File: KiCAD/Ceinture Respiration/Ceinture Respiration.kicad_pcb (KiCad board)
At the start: 2 copper layers, 124 x 55 mm, 37 parts, among them J1 DIN-8, J2 DIN-8, J3 Conn_01x04, J4 MEM2061-01-188-00-A_REVA, J5 Conn_01x02, J7 Conn_01x10_Pin, J8 Conn_01x10_Socket, Q1 MMBT3904, Q2 MMBT3904, SW1 SW_Push, SW2 SW_Push, SW3 SW_Push, SW4 SW_Push

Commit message: Schématique prête pour design review
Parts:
- removed C2: 10uF, Capacitor_SMD:C_0603_1608Metric
- removed D6: GREEN, LED_THT:LED_D3.0mm
- removed D7: D_Schottky, Diode_SMD:D_SOD-123
- removed J3: Conn_01x04, Connector_PinSocket_2.54mm:PinSocket_1x04_P2.54mm_Vertical
- removed J8: Conn_01x10_Socket, Connector_PinSocket_2.54mm:PinSocket_2x05_P2.54mm_Horizontal
- removed Q2: MMBT3904, Package_TO_SOT_SMD:SOT-23
- removed R3: 10K, Resistor_SMD:R_0603_1608Metric
- removed R6, R9: 1K, Resistor_SMD:R_0603_1608Metric
- added C3: 1u, Capacitor_SMD:C_0402_1005Metric, F.Cu at (80.6, 38.2)
- added C4: 1u, Capacitor_SMD:C_0402_1005Metric, F.Cu at (80.6, 40.2)
- added J6: MEM2061-01-188-00-A_REVA, CentureResp:GCT_MEM2061-01-188-00-A_REVA, F.Cu at (79.8, 28.7)
- added J9: Oled, CentureResp:Adafruit_SSD1306_SPI, F.Cu at (44.5, 23.8)
- added U1: DRV2605LDGS, Package_SO:VSSOP-10_3x3mm_P0.5mm, F.Cu at (75.4, 39.5)
- D2: value DIODE -> D_Schottky
- D5: value ORANGE -> GREEN
- J2: value DIN-8 -> Conn_01x10_Socket
- J4: value MEM2061-01-188-00-A_REVA -> DIN-8
- J5: value Conn_01x02 -> BUZZER
- J7: value Conn_01x10_Pin -> Conn_01x02_Socket
- R2: value 10K -> 1K
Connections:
- net /BATT_VOLTAGE renamed /MCU/bat_voltage
- net /BUZZER renamed /DEVICES/BUZZER
- net /LED1 renamed /DEVICES/LED1
- net /LED2 renamed /EXT3
- net /Signal_1 renamed /MCU/EXT1
- net /Signal_2 renamed /MCU/EXT2
- A1 pad 10: unconnected-(A1-D7-Pad10) -> /DEVICES/OLED_CS
- A1 pad 11: /BTN3 -> /DEVICES/BTN4
- A1 pad 12: /BTN4 -> /DEVICES/OLED_DC
- A1 pad 13: /SD_CS -> /DEVICES/SD_CS
- A1 pad 22: unconnected-(A1-A3-Pad22) -> /DEVICES/BTN3
- A1 pad 25: /BTN1 -> /DEVICES/BTN1
- A1 pad 26: /BTN2 -> /DEVICES/BTN2
- A1 pad 7: /LED3 -> /DEVICES/SD_DETECT
- A1 pad 9: /MOTOR -> /DEVICES/OLED_RST
- BT1 pad +: Net-(D7-A) -> Net-(D2-A)
- C1 pad 1: /BUZZER_P -> Net-(D1-A)
- D1 pad 2: /BUZZER_P -> Net-(D1-A)
- D2 pad 1: GND -> Net-(D2-K)
- D2 pad 2: /MOTOR_P -> Net-(D2-A)
- D3 pad 2: /PWR_LED -> /SHIELD_RESPIRATION/PWR_LED
- J1 pad 3: /Belt_1 -> /SHIELD_RESPIRATION/Belt_1
- J2 pad 1: +5VA -> +BATT
- J2 pad 2: unconnected-(J2-Pad2) -> GND1
- J2 pad 3: /Belt_2 -> /SHIELD_RESPIRATION/Belt_1
- J2 pad 4: -5VA -> /SHIELD_RESPIRATION/Belt_2
- J2 pad 7: GND1 -> unconnected-(J2-Pin_7-Pad7)
- J4 pad 1: Net-(J4-DAT2) -> +5VA
- J4 pad 10: unconnected-(J4-CD2-Pad10) -> (no net)
- J4 pad 11: GND -> (no net)
- J4 pad 12: GND -> (no net)
- J4 pad 2: /SD_CS -> unconnected-(J4-Pad2)
- J4 pad 3: /MOSI -> /SHIELD_RESPIRATION/Belt_2
- J4 pad 4: +3.3V -> -5VA
- J4 pad 5: /SCK -> unconnected-(J4-Pad5)
- J4 pad 6: GND -> unconnected-(J4-Pad6)
- J4 pad 7: /MISO -> GND1
- J4 pad 8: Net-(J4-DAT1) -> unconnected-(J4-Pad8)
- J4 pad 9: unconnected-(J4-CD1-Pad9) -> (no net)
- J5 pad 1: /BUZZER_P -> GND
- J5 pad 2: GND -> Net-(D1-A)
- J7 pad 1: /A1 -> GND
- J7 pad 10: unconnected-(J7-Pin_10-Pad10) -> (no net)
- J7 pad 2: /A2 -> VDD
- J7 pad 3: VDD -> (no net)
- J7 pad 4: GND -> (no net)
- J7 pad 5: unconnected-(J7-Pin_5-Pad5) -> (no net)
- J7 pad 6: unconnected-(J7-Pin_6-Pad6) -> (no net)
- J7 pad 7: unconnected-(J7-Pin_7-Pad7) -> (no net)
- J7 pad 8: unconnected-(J7-Pin_8-Pad8) -> (no net)
- J7 pad 9: unconnected-(J7-Pin_9-Pad9) -> (no net)
- Q1 pad 2: /BUZZER_P -> Net-(D1-A)
- Q1 pad 3: +5V -> +3.3V
- R2 pad 1: /MOTOR -> /SHIELD_RESPIRATION/PWR_LED
- R2 pad 2: Net-(Q2-B) -> +5VA
- R4 pad 2: Net-(J4-DAT2) -> Net-(J6-DAT2)
- R5 pad 2: Net-(J4-DAT1) -> Net-(J6-DAT1)
- S1 pad S: Net-(D7-K) -> Net-(D2-K)
- SW1 pad 1: /BTN3 -> /DEVICES/BTN1
- SW2 pad 1: /BTN1 -> /DEVICES/BTN2
- SW3 pad 1: /BTN2 -> /DEVICES/BTN3
- SW4 pad 1: /BTN4 -> /DEVICES/BTN4

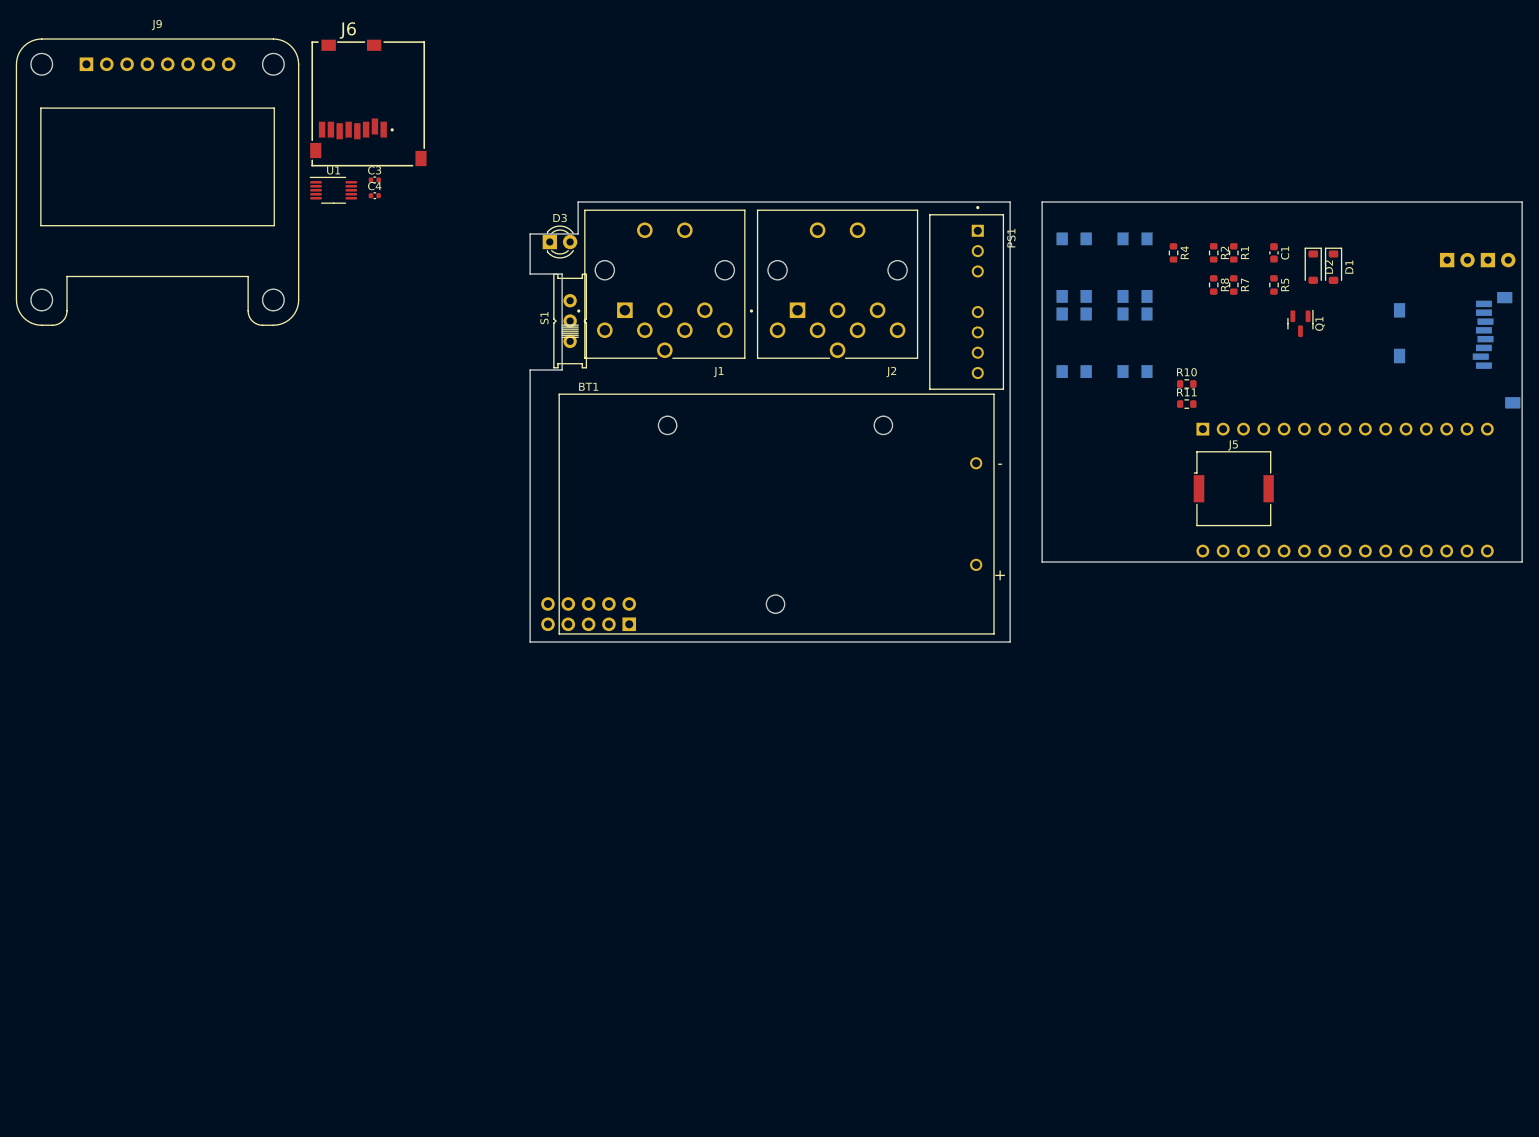
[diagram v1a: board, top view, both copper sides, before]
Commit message: Schematique 99%, PCB 50%
schématique complété, nettoyé et layout complété, reste routage
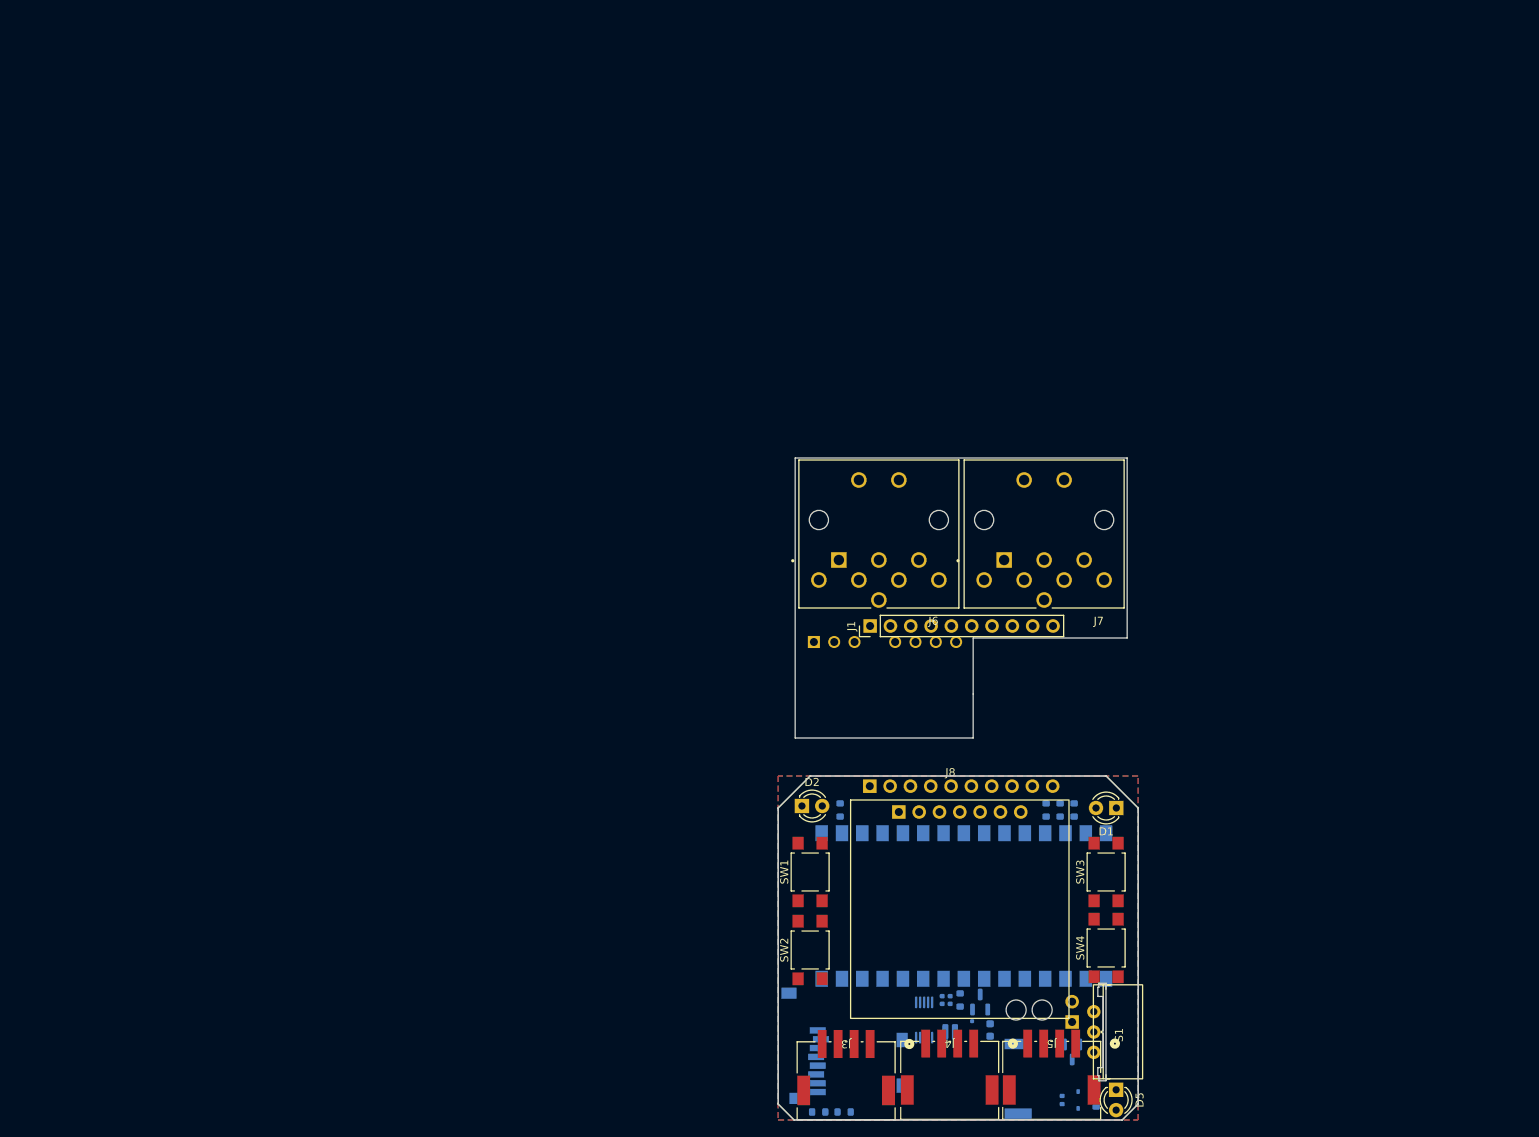
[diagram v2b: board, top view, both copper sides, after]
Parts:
- removed BT1: BH9VPC, CentureResp:BAT_BH9VPC
- removed C4: 1u, Capacitor_SMD:C_0402_1005Metric
- removed R10: 10K, Resistor_SMD:R_0603_1608Metric
- removed R11: 1K, Resistor_SMD:R_0603_1608Metric
- added C2: 1u, Capacitor_SMD:C_0402_1005Metric, B.Cu at (151.5, 140.8)
- added J10: BUZZER, CentureResp:Buzzer_Murata_PKMCS0909E, B.Cu at (161.0, 150.6)
- added J11: Conn_01x02, Connector_PinHeader_2.54mm:PinHeader_1x02_P2.54mm_Vertical, B.Cu at (167.8, 143.5)
- added J3: Conn_01x06_Pin, CentureResp:CONN4_20164_SEE, F.Cu at (142.5, 146.2)
- added J8: Oled, CentureResp:Adafruit_SSD1306_SPI, F.Cu at (153.7, 117.2)
- added M1: Motor_DC, CentureResp:XDCR_C0720B001F, B.Cu at (152.5, 149.8)
- added Q2: AP10N04S, Package_TO_SOT_SMD:SOT-23, B.Cu at (167.8, 147.2)
- added R3: 1K, Resistor_SMD:R_0603_1608Metric, B.Cu at (168.0, 117.0)
- added R6: 10K, Resistor_SMD:R_0603_1608Metric, B.Cu at (136.1, 154.8)
- added R9: 1K, Resistor_SMD:R_0603_1608Metric, B.Cu at (170.8, 153.2)
- A1: footprint Module:Arduino_Nano -> CentureResp:MODULE_ABX00027
- C1, C3, PS1, Q1, R1, R2, R5, U1: moved to B.Cu
- D1: value DIODE -> RED; footprint Diode_SMD:D_SOD-123 -> LED_THT:LED_D3.0mm
- D2: value D_Schottky -> GREEN; footprint Diode_SMD:D_SOD-123 -> LED_THT:LED_D3.0mm
- D3: value LED -> D; footprint LED_THT:LED_D3.0mm -> Diode_SMD:D_SOD-323F; moved to B.Cu
- D4: value RED -> 6-12V; footprint LED_THT:LED_D3.0mm -> Diode_SMD:D_SOD-323
- D5: value GREEN -> LED; moved to F.Cu
- J1: value DIN-8 -> Conn_01x10_Pin; footprint CentureResp:CUI_SDS-80J -> Connector_PinHeader_2.54mm:PinHeader_1x10_P2.54mm_Vertical
- J2: footprint CentureResp:CUI_SDS-80J -> Connector_PinSocket_2.54mm:PinSocket_1x10_P2.54mm_Vertical; moved to B.Cu
- J4: value DIN-8 -> Conn_01x06_Pin; footprint CentureResp:GCT_MEM2061-01-188-00-A_REVA -> CentureResp:CONN4_20164_SEE; moved to F.Cu
- J5: value BUZZER -> Conn_01x06_Pin; footprint Buzzer_Beeper:Buzzer_Murata_PKMCS0909E -> CentureResp:CONN4_20164_SEE
- J6: value MEM2061-01-188-00-A_REVA -> DIN-8; footprint CentureResp:GCT_MEM2061-01-188-00-A_REVA -> CentureResp:CUI_SDS-80J
- J7: value Conn_01x02_Socket -> DIN-8; footprint Connector_PinHeader_2.54mm:PinHeader_2x05_P2.54mm_Horizontal -> CentureResp:CUI_SDS-80J; moved to F.Cu
- J9: value Oled -> MEM2061-01-188-00-A_REVA; footprint CentureResp:Adafruit_SSD1306_SPI -> CentureResp:GCT_MEM2061-01-188-00-A_REVA; moved to B.Cu
- R4: value 10K -> 1K; moved to B.Cu
- R7: value 1K -> 10K; moved to B.Cu
- R8: value 1K -> 10K; footprint Resistor_SMD:R_0603_1608Metric -> Resistor_SMD:R_0402_1005Metric; moved to B.Cu
- SW1, SW2, SW3, SW4: moved to F.Cu
- moved J9 155.0 mm to (139.2, 146.5), turned to 90 degrees
- moved U1 127.3 mm to (149.2, 143.2), turned to -90 degrees
- moved C3 125.2 mm to (152.5, 140.8), turned to -90 degrees
- moved D4 116.8 mm to (168.5, 153.2), turned to -90 degrees
- moved R5 116.5 mm to (139.2, 154.8), turned to 180 degrees
- moved D3 111.8 mm to (155.2, 144.5), turned to -90 degrees
- moved D5 111.7 mm to (173.2, 152.0), turned to -90 degrees
- moved S1 110.4 mm to (170.5, 144.8), turned to -90 degrees
- moved J4 105.8 mm to (155.4, 146.2), turned to 180 degrees
- moved R8 103.6 mm to (166.5, 153.2), turned to 90 degrees
- moved C1 103.4 mm to (157.5, 144.5)
- moved R7 95.7 mm to (153.8, 140.8)
- moved SW2 94.5 mm to (135.0, 134.5), turned to 90 degrees
- moved Q1 93.8 mm to (156.2, 141.0), turned to 90 degrees
- moved D2 92.9 mm to (134.0, 116.5), turned to 0 degrees
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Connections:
- A1 pad 1: unconnected-(A1-D1/TX-Pad1) -> /DEVICES/BTN3
- A1 pad 11: /DEVICES/BTN4 -> /DEVICES/BUZZER
- A1 pad 14: /MOSI -> /DEVICES/MOSI
- A1 pad 15: /MISO -> /DEVICES/MISO
- A1 pad 16: /SCK -> /DEVICES/SCK
- A1 pad 2: unconnected-(A1-D0/RX-Pad2) -> /DEVICES/BTN4
- A1 pad 22: /DEVICES/BTN3 -> /MCU/EXT3
- A1 pad 30: VDD -> /BATTERIE 9V/VBAT
- A1 pad 6: /EXT3 -> /DEVICES/LED2
- A1 pad 8: /DEVICES/BUZZER -> /MCU/EXT4
- C1 pad 1: Net-(D1-A) -> Net-(D3-K)
- C3 pad 1: +3.3V -> /DEVICES/M_REG
- D2 pad 1: Net-(D2-K) -> GND
- D3 pad 1: GND1 -> Net-(D3-K)
- D3 pad 2: /SHIELD_RESPIRATION/PWR_LED -> GND
- D4 pad 1: GND -> Net-(D4-K)
- D4 pad 2: Net-(D4-A) -> /BATTERIE 9V/24V_PROT_GATE
- J1 pad 1: +5VA -> GND_EXP
- J1 pad 2: unconnected-(J1-Pad2) -> /SHIELD_RESPIRATION/VBAT_EXP
- J1 pad 4: -5VA -> /SHIELD_RESPIRATION/Belt_2
- J1 pad 7: GND1 -> unconnected-(J1-Pin_7-Pad7)
- J2 pad 1: +BATT -> GND
- J2 pad 2: GND1 -> /BATTERIE 9V/VBAT
- J2 pad 3: /SHIELD_RESPIRATION/Belt_1 -> /MCU/EXT1
- J2 pad 4: /SHIELD_RESPIRATION/Belt_2 -> /MCU/EXT2
- J2 pad 5: unconnected-(J2-Pin_5-Pad5) -> /MCU/EXT3
- J2 pad 6: unconnected-(J2-Pin_6-Pad6) -> /MCU/EXT4
- J2 pad 7: unconnected-(J2-Pin_7-Pad7) -> /SDA
- J2 pad 8: unconnected-(J2-Pin_8-Pad8) -> /SCL
- J4 pad 1: +5VA -> /MCU/EXT3
- J4 pad 2: unconnected-(J4-Pad2) -> /MCU/EXT4
- J4 pad 3: /SHIELD_RESPIRATION/Belt_2 -> +5V
- J4 pad 4: -5VA -> GND
- J4 pad 5: unconnected-(J4-Pad5) -> GND
- J4 pad 6: unconnected-(J4-Pad6) -> GND
- J5 pad 1: GND -> /SCL
- J5 pad 2: Net-(D1-A) -> /SDA
- J6 pad 1: Net-(J6-DAT2) -> +5VA
- J6 pad 2: /DEVICES/SD_CS -> unconnected-(J6-Pad2)
- J6 pad 3: /MOSI -> /SHIELD_RESPIRATION/Belt_1
- J6 pad 4: +3.3V -> -5VA
- J6 pad 5: /SCK -> unconnected-(J6-Pad5)
- J6 pad 6: GND -> unconnected-(J6-Pad6)
- J6 pad 7: /MISO -> GND_EXP
- J6 pad 8: Net-(J6-DAT1) -> unconnected-(J6-Pad8)
- J7 pad 1: GND -> +5VA
- J7 pad 2: VDD -> unconnected-(J7-Pad2)
- J7 pad 3: (no net) -> /SHIELD_RESPIRATION/Belt_2
- J7 pad 4: (no net) -> -5VA
- J7 pad 5: (no net) -> unconnected-(J7-Pad5)
- J7 pad 6: (no net) -> unconnected-(J7-Pad6)
- J7 pad 7: (no net) -> GND_EXP
- J7 pad 8: (no net) -> unconnected-(J7-Pad8)
- J9 pad 1: GND -> Net-(J9-DAT2)
- J9 pad 2: +3.3V -> /DEVICES/SD_CS
- J9 pad 3: /SCK -> /DEVICES/MOSI
- J9 pad 4: /MOSI -> +3.3V
- J9 pad 5: /DEVICES/OLED_RST -> /DEVICES/SCK
- J9 pad 6: /DEVICES/OLED_DC -> GND
- J9 pad 7: /DEVICES/OLED_CS -> /DEVICES/MISO
- J9 pad 8: (no net) -> Net-(J9-DAT1)
- PS1 pad 1: GND1 -> GND_EXP
- PS1 pad 2: +BATT -> /SHIELD_RESPIRATION/VBAT_EXP
- PS1 pad 3: GND1 -> GND_EXP
- PS1 pad 7: GND1 -> GND_EXP
- Q1 pad 2: Net-(D1-A) -> Net-(D3-K)
- R1 pad 1: /DEVICES/BUZZER -> /BATTERIE 9V/VBAT
- R1 pad 2: Net-(Q1-B) -> /MCU/bat_voltage
- R2 pad 1: /SHIELD_RESPIRATION/PWR_LED -> /MCU/bat_voltage
- R2 pad 2: +5VA -> GND
- R4 pad 1: +3.3V -> Net-(D2-A)
- R4 pad 2: Net-(J6-DAT2) -> /DEVICES/LED2
- R5 pad 2: Net-(J6-DAT1) -> Net-(J9-DAT2)
- R7 pad 1: Net-(D4-A) -> /DEVICES/BUZZER
- R7 pad 2: /DEVICES/LED1 -> Net-(Q1-B)
- R8 pad 1: Net-(D5-A) -> /BATTERIE 9V/24V_PROT_GATE
- R8 pad 2: /EXT3 -> GND
- S1 pad O: unconnected-(S1-PadO) -> /BATTERIE 9V/VBAT
- S1 pad P: +BATT -> Net-(D4-K)
- S1 pad S: Net-(D2-K) -> unconnected-(S1-PadS)
- U1 pad 6: (no net) -> +3.3V
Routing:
- added copper zone on B.Cu, net GND
- added copper zone on F.Cu, net GND
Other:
- board size 124 x 55 mm -> 45 x 82.8 mm

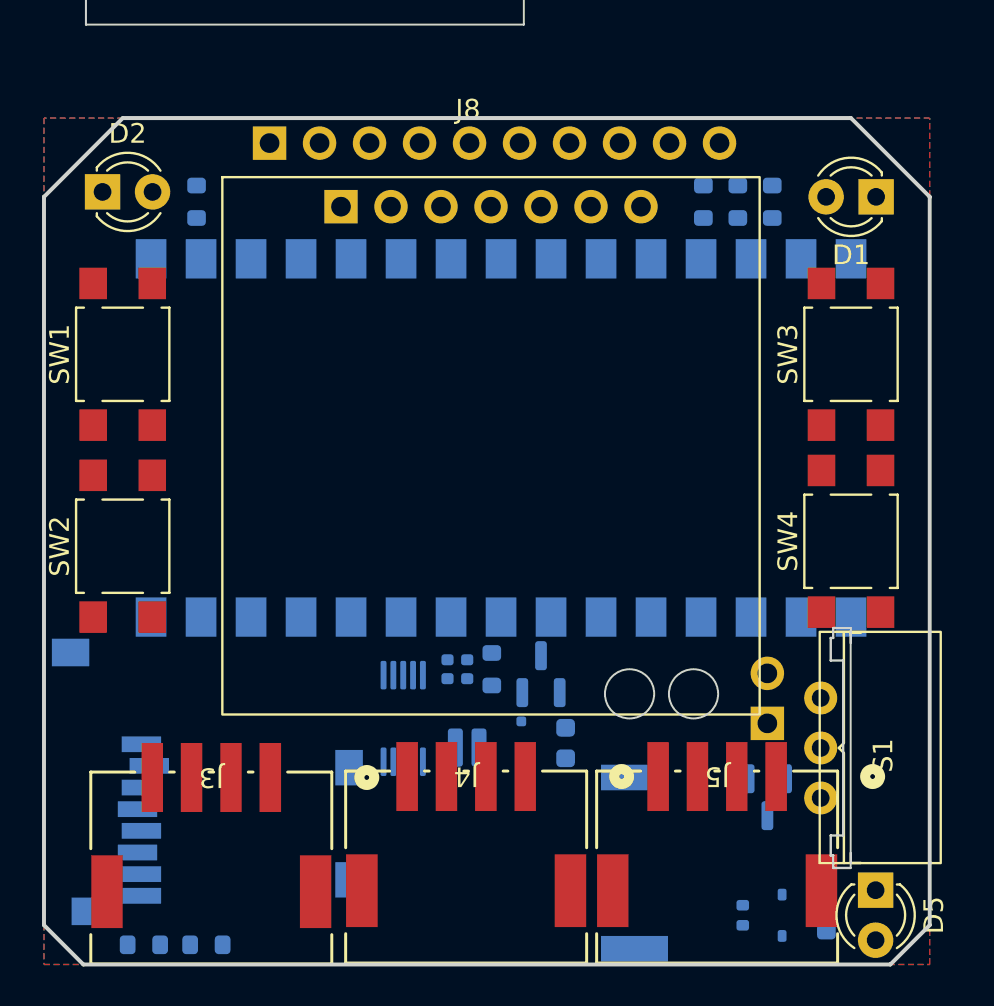
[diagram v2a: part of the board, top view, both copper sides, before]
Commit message: sch 99% pcb 85%
Ajout de l'ensemble des traces du pcb mère
Ajout de via stiching
Reste le PCB shield à terminer
Reste les erreurs générés à nettoyer
Brûlé le gars...
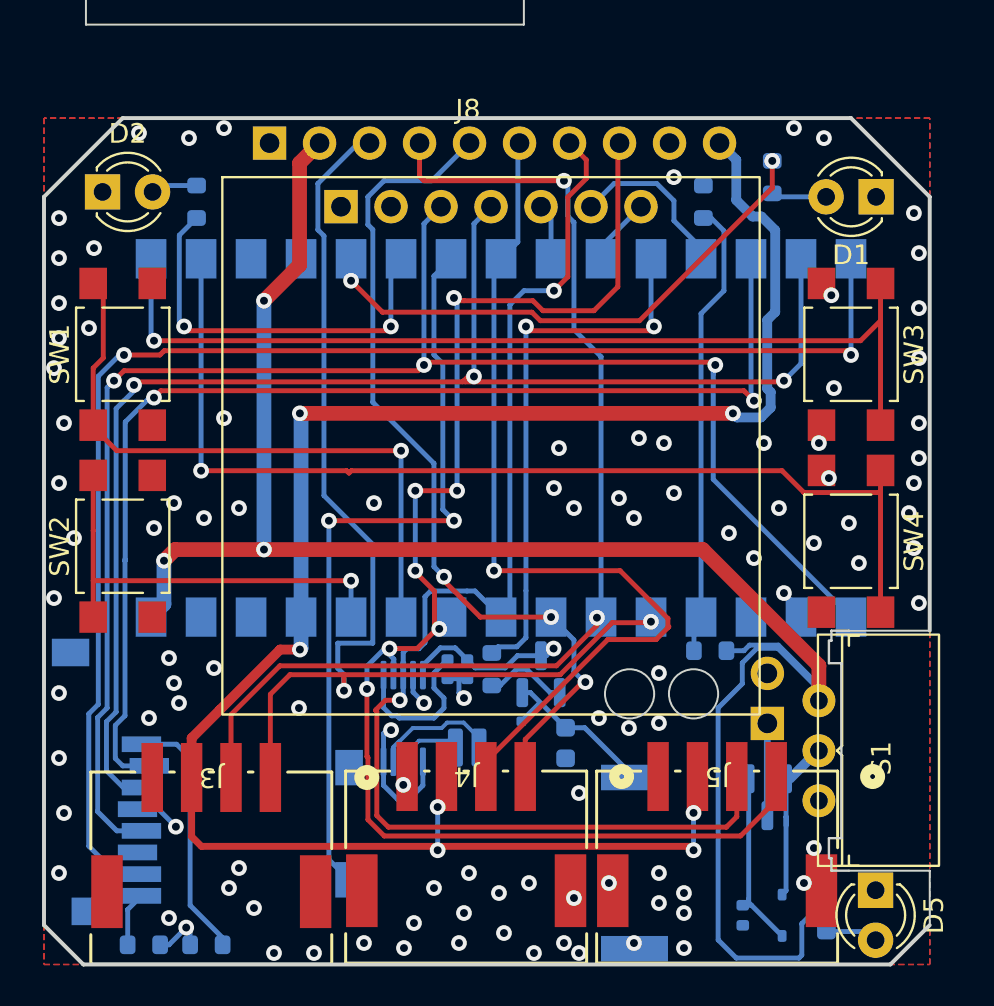
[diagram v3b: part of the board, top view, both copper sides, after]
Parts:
- moved R1 22.9 mm to (164.8, 139.8), turned to 180 degrees
- moved R3 1.25 mm to (168.0, 115.8)
- moved C2 1.00 mm to (152.5, 140.8)
- moved C3 1.00 mm to (151.5, 140.8)
- moved S1 0.16 mm to (170.4, 144.9)
- turned R2 to 90 degrees
- turned R5 to 0 degrees
- turned R8 to -90 degrees
- turned SW3 to -90 degrees
- turned SW4 to -90 degrees
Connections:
- net Net-(D4-K) renamed /BATTERIE 9V/BAT+_PROT
- net Net-(J11-Pin_1) renamed /BATTERIE 9V/BAT+
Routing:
- net +5V: track 0.00 -> 97.4 mm, vias 0 -> 7
- net /BATTERIE 9V/VBAT: track 0.00 -> 97.4 mm, vias 0 -> 3
- net /DEVICES/SCK: track 0.00 -> 80.0 mm, vias 0 -> 3
- net /SCL: track 0.00 -> 72.8 mm, vias 0 -> 7
- net /DEVICES/MOSI: track 0.00 -> 71.6 mm, vias 0 -> 3
- net /DEVICES/MISO: track 0.00 -> 71.2 mm, vias 0 -> 2
- net /SDA: track 0.00 -> 65.4 mm, vias 0 -> 2
- net /DEVICES/SD_CS: track 0.00 -> 59.4 mm, vias 0 -> 2
- net /MCU/EXT1: track 0.00 -> 58.4 mm, vias 0 -> 2
- net /MCU/EXT2: track 0.00 -> 57.0 mm, vias 0 -> 2
- net /DEVICES/BTN4: track 0.00 -> 53.1 mm, vias 0 -> 1
- net /DEVICES/BTN3: track 0.00 -> 48.8 mm, vias 0 -> 1
- net /MCU/EXT4: track 0.00 -> 45.5 mm, vias 0 -> 1
- net /MCU/EXT3: track 0.00 -> 43.9 mm, vias 0 -> 3
- net /DEVICES/SD_DETECT: track 0.00 -> 39.1 mm, vias 0 -> 2
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- added copper zone on In2.Cu, net +3.3V
- added copper zone on In1.Cu, net GND
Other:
- outline, holes or cut-outs redrawn
- copper layers 2 -> 4
